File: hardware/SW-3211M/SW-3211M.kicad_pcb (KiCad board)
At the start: 2 copper layers, 65 x 25 mm, 41 parts, among them J1 Conn_01x07, J2 STX-3100-5N, J3 Conn_01x03, Q1 NTF2955, Q2 DMN2041L, Q3 DMN2041L, T1 42TL004-RC, U1 LMC6482

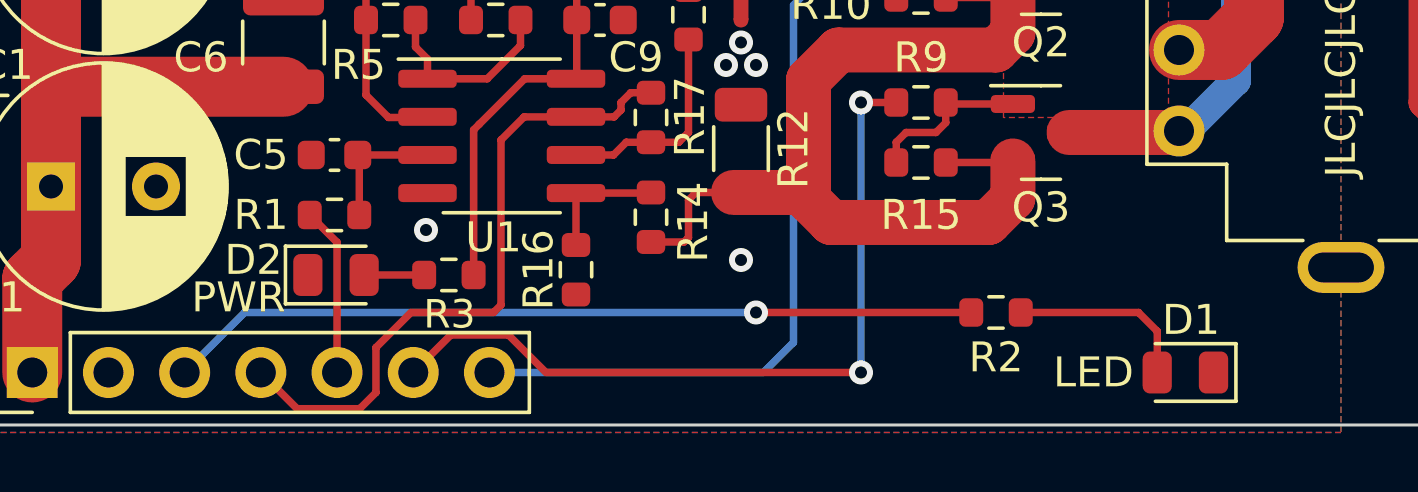
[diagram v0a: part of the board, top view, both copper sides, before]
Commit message: update part numbers
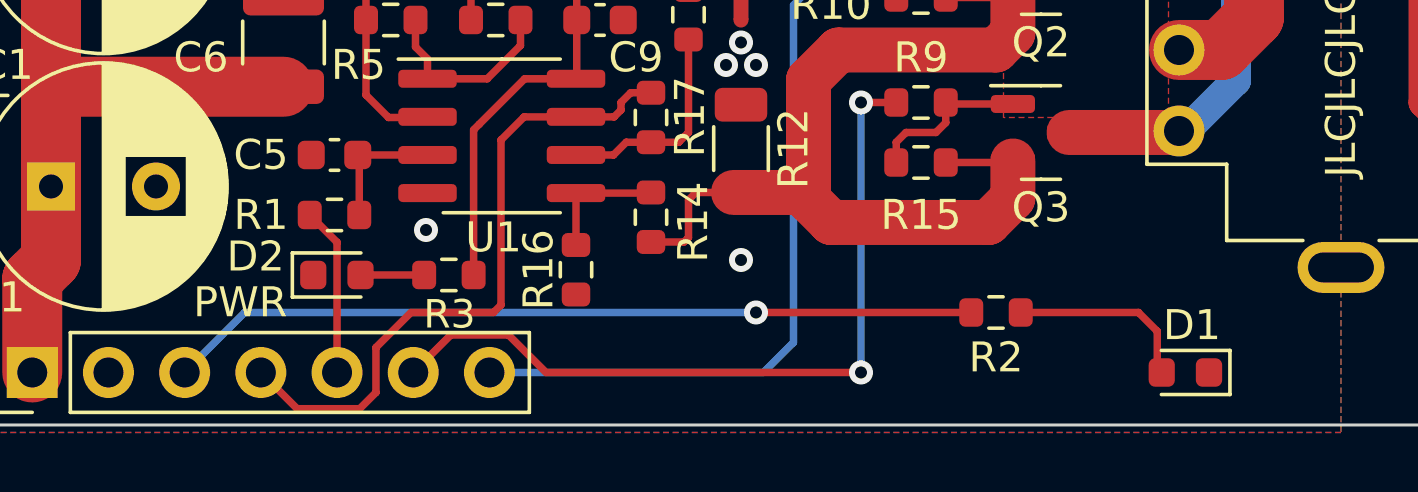
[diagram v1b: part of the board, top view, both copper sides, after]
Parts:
- D1, D2: footprint LED_SMD:LED_0805_2012Metric -> LED_SMD:LED_0603_1608Metric
- R2, R3: value 330 -> 470
- U1: value LMC6482 -> TLV272IS-13
